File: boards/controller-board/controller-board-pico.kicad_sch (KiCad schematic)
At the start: 62 parts, among them J1 Phoenix 1935161, J2 Conn_01x02, J3 Conn_01x02, J4 Conn_01x02, J5 Conn_01x03, J6 Phoenix 1935161, J7 Conn_01x03, J8 Conn_01x03, Q1 PMV45EN, Q2 Goford_G11S_20V_11A, U2 ADS1015IRUGR, U4 RPi_Pico, U5 MCP4728

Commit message: rm photodiode, switch power terminals, 2->1 fans
* No longer using the sensor boards will just move direct connections with
thermisters taped down on bottom stand.

* Switch screw terminals to banana jacks and added jank symbol, stil WIP
  on the footprint

* Change from two smaller fans to one larger overhead fan, removing the
  drawings of the outer wings
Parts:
- removed J1: Phoenix 1935161, TerminalBlock_Phoenix:TerminalBlock_Phoenix_PT-1,5-2-5.0-H_1x02_P5.00mm_Horizontal, symbol Connector_Generic:Conn_01x02
- removed J5, J8: Conn_01x03, Connector_PinHeader_2.54mm:PinHeader_1x03_P2.54mm_Vertical, symbol Connector_Generic:Conn_01x03
- removed TP5: TestPoint-MinTH, oresat-misc:TestPoint-MinTH, symbol oresat-misc:TestPoint-MinTH
- added P1: Banana Jack V_IN, symbol controller-brd:Conn_Plug_1P
- added P2: Banana Jack GND, symbol controller-brd:Conn_Plug_1P
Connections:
- net GND: now also P2.1 (P)
- net at F1.2, F2.2, TP1.1: now also P1.1 (P)
- net PHOTODIODE: no longer names the net of U2.7 (AIN3)
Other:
- note added: "10k THT Thermistor"
- note added: "12 V Fan"
- note added: "FAN"
- note added: "Measured 12V @ 17A Rated 24A"
- note removed: "12 V Fans"
- note removed: "12V @ 11A"
- note removed: "L FAN"
- note removed: "Photodiode"
- note removed: "R FAN"
- moved on the sheet: C15, C17, C18, C19, C4, D19, F1, F2, F3, F4, HW1, HW2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

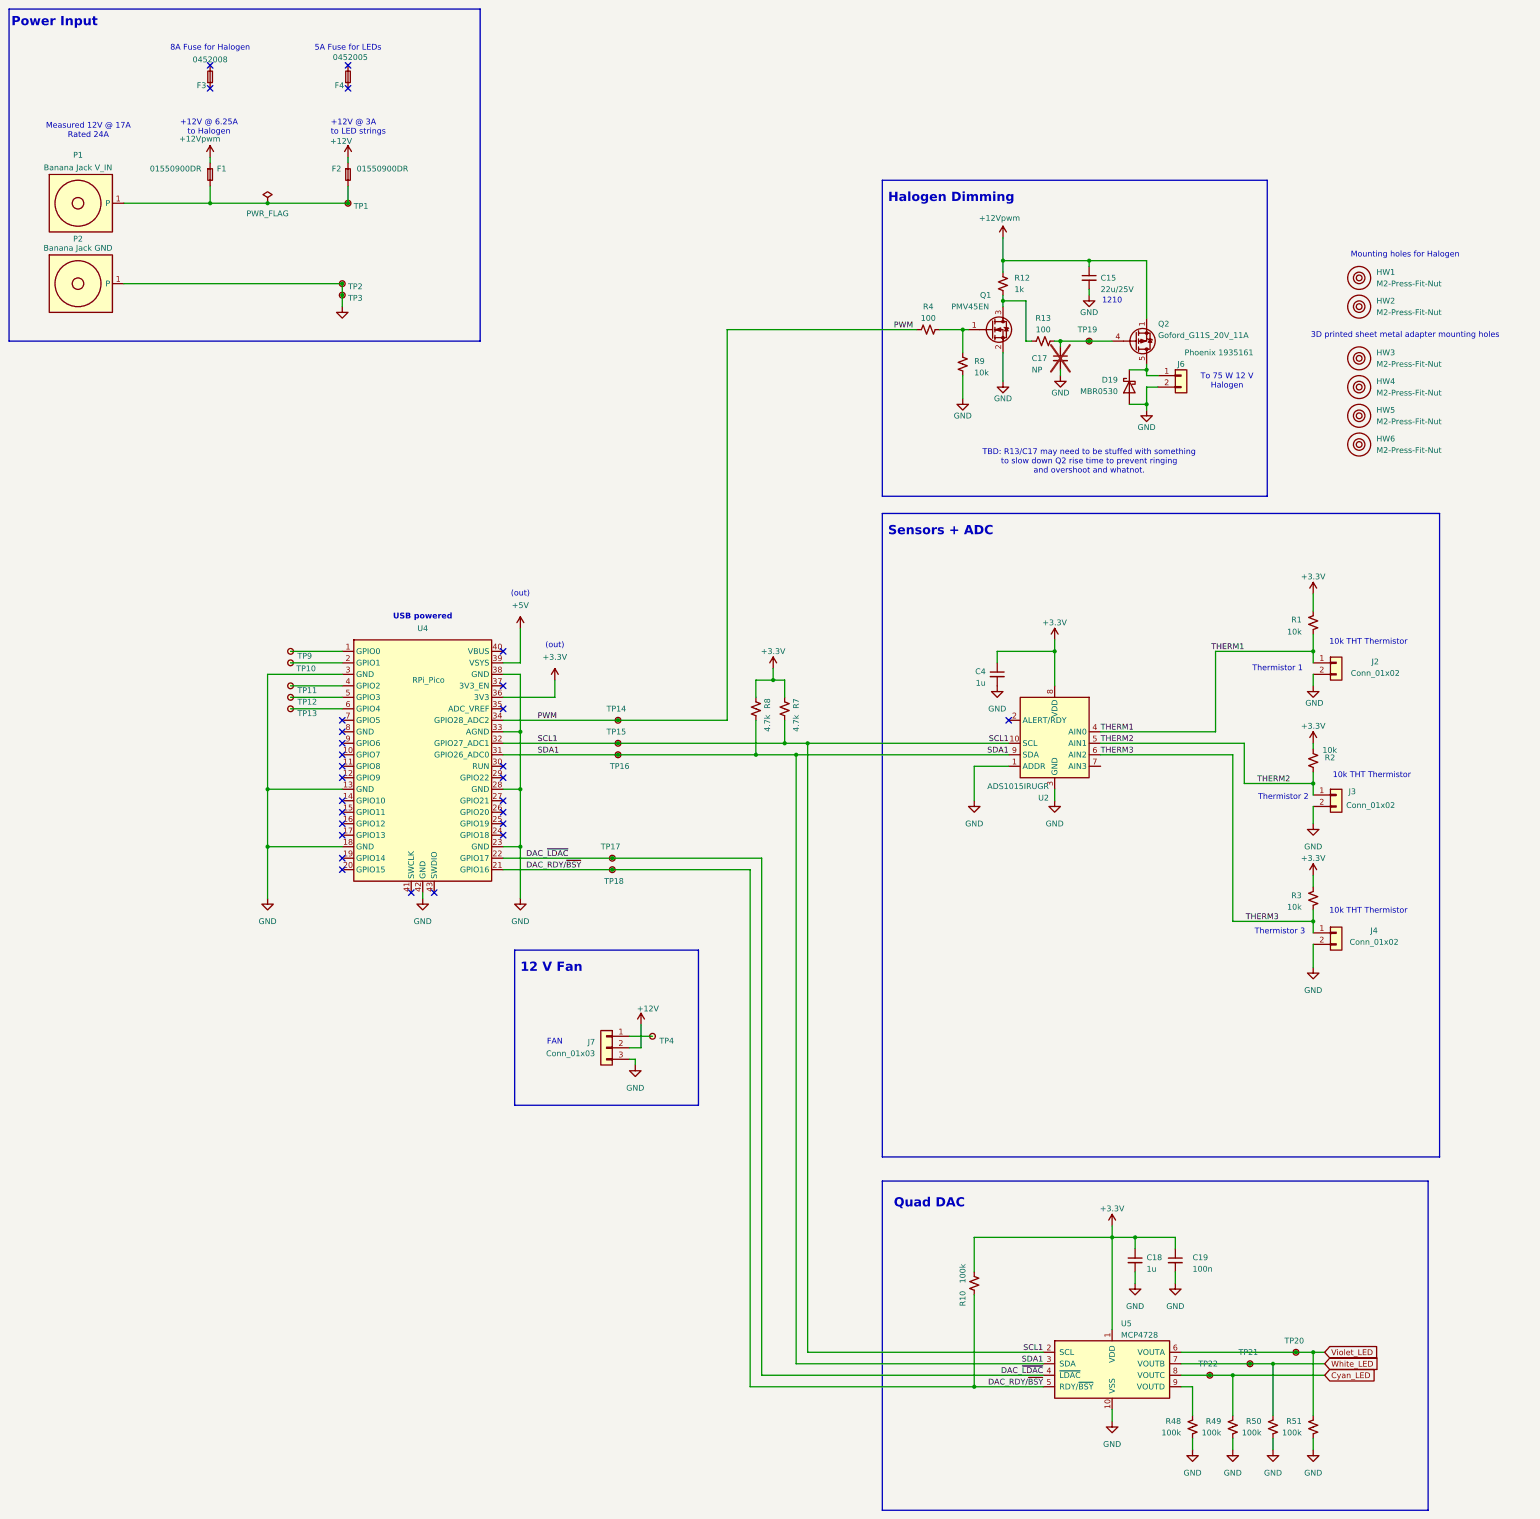
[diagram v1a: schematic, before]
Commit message: Change MCU, Power terminal, and relayout PCB
* From a pi pico we change to a RP-2040 xiao MCU which has smaller
footprint and USB-C
* Remove the previously added banana cables and go with 6PIN molex
receptacle to match the needed 12V DC powersupply we intend to use.
* With the above changes relaid out the PCB
  - No current ERC nor DRC errors of note
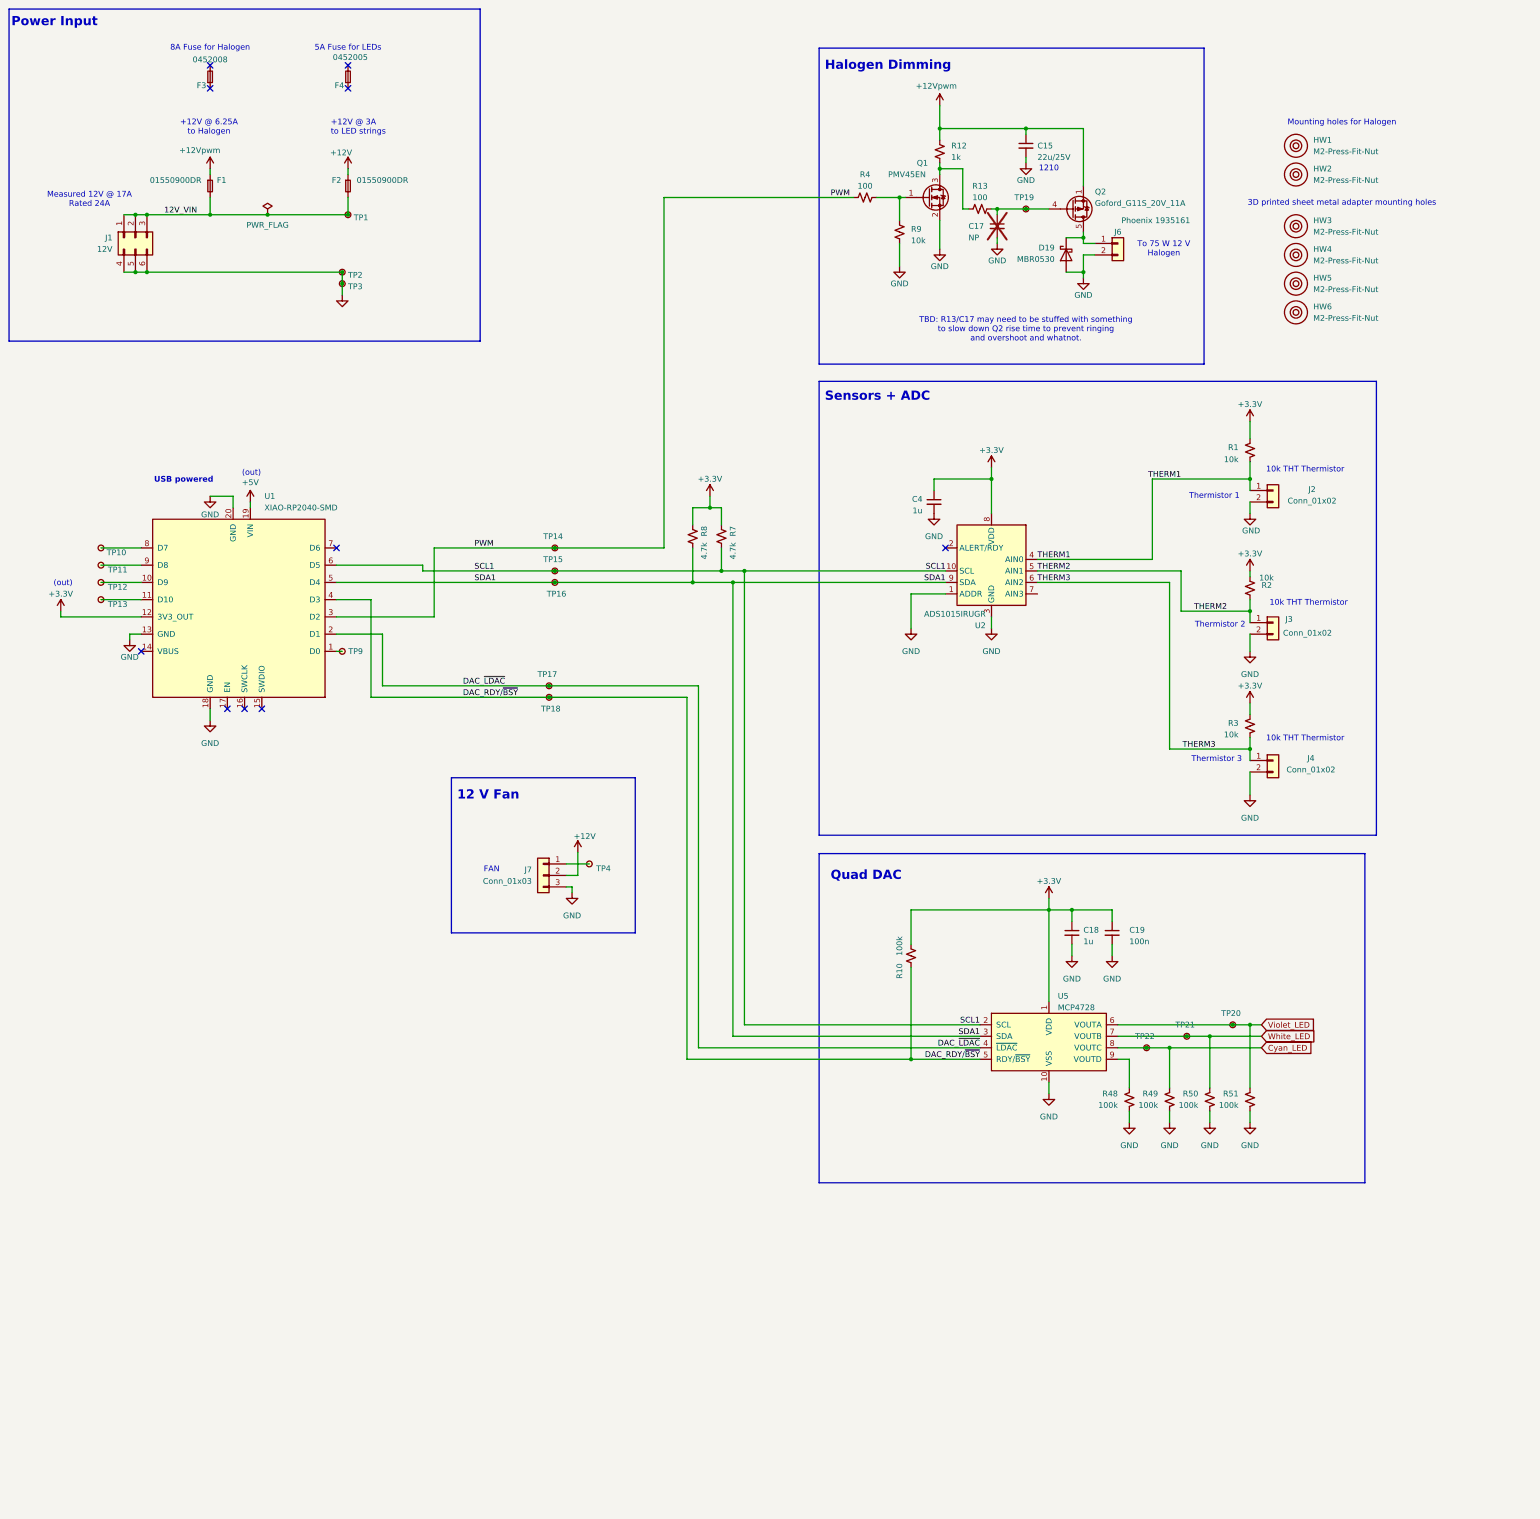
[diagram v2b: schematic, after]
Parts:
- removed P1: Banana Jack V_IN, symbol controller-brd:Conn_Plug_1P
- removed P2: Banana Jack GND, symbol controller-brd:Conn_Plug_1P
- removed U4: RPi_Pico, oresat-misc:Raspberry Pi Pico Castellated, symbol oresat-misc:RPi_Pico
- added J1: 12V, controller_brd_footprints:CONN_6P_RECPT, symbol Connector_Generic:Conn_02x03_Top_Bottom
- added U1: XIAO-RP2040-SMD, controller_brd_footprints:XIAO-RP2040-SMD, symbol controller-brd:XIAO-RP2040-SMD
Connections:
- net +3.3V: now also U1.12 (3V3_OUT)
- net +5V: now also U1.19 (VIN)
- net DAC_RDY/~{BSY}: now also U1.4 (D3)
- net DAC_~{LDAC}: now also U1.2 (D1)
- net GND: now also J1.4 (Pin_4), J1.5 (Pin_5), J1.6 (Pin_6), U1.13 (GND), U1.18 (GND), U1.20 (GND)
- net PWM: now also U1.3 (D2)
- net SCL1: now also U1.6 (D5)
- net SDA1: now also U1.5 (D4)
- net 12V_VIN: now reaches F1.2, F2.2, TP1.1
- net 12V_VIN: now also J1.1 (Pin_1), J1.2 (Pin_2), J1.3 (Pin_3)
- net at TP11.1: now also U1.9 (D8)
- net at TP12.1: now also U1.10 (D9)
- net at TP9.1: now also U1.1 (D0)
- net at TP10.1: now also U1.8 (D7)
- net at TP13.1: now also U1.11 (D10)
- no-connect marks 28 -> 10
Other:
- moved on the sheet: C15, C17, C18, C19, C4, D19, F1, F2, HW1, HW2, HW3, HW4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

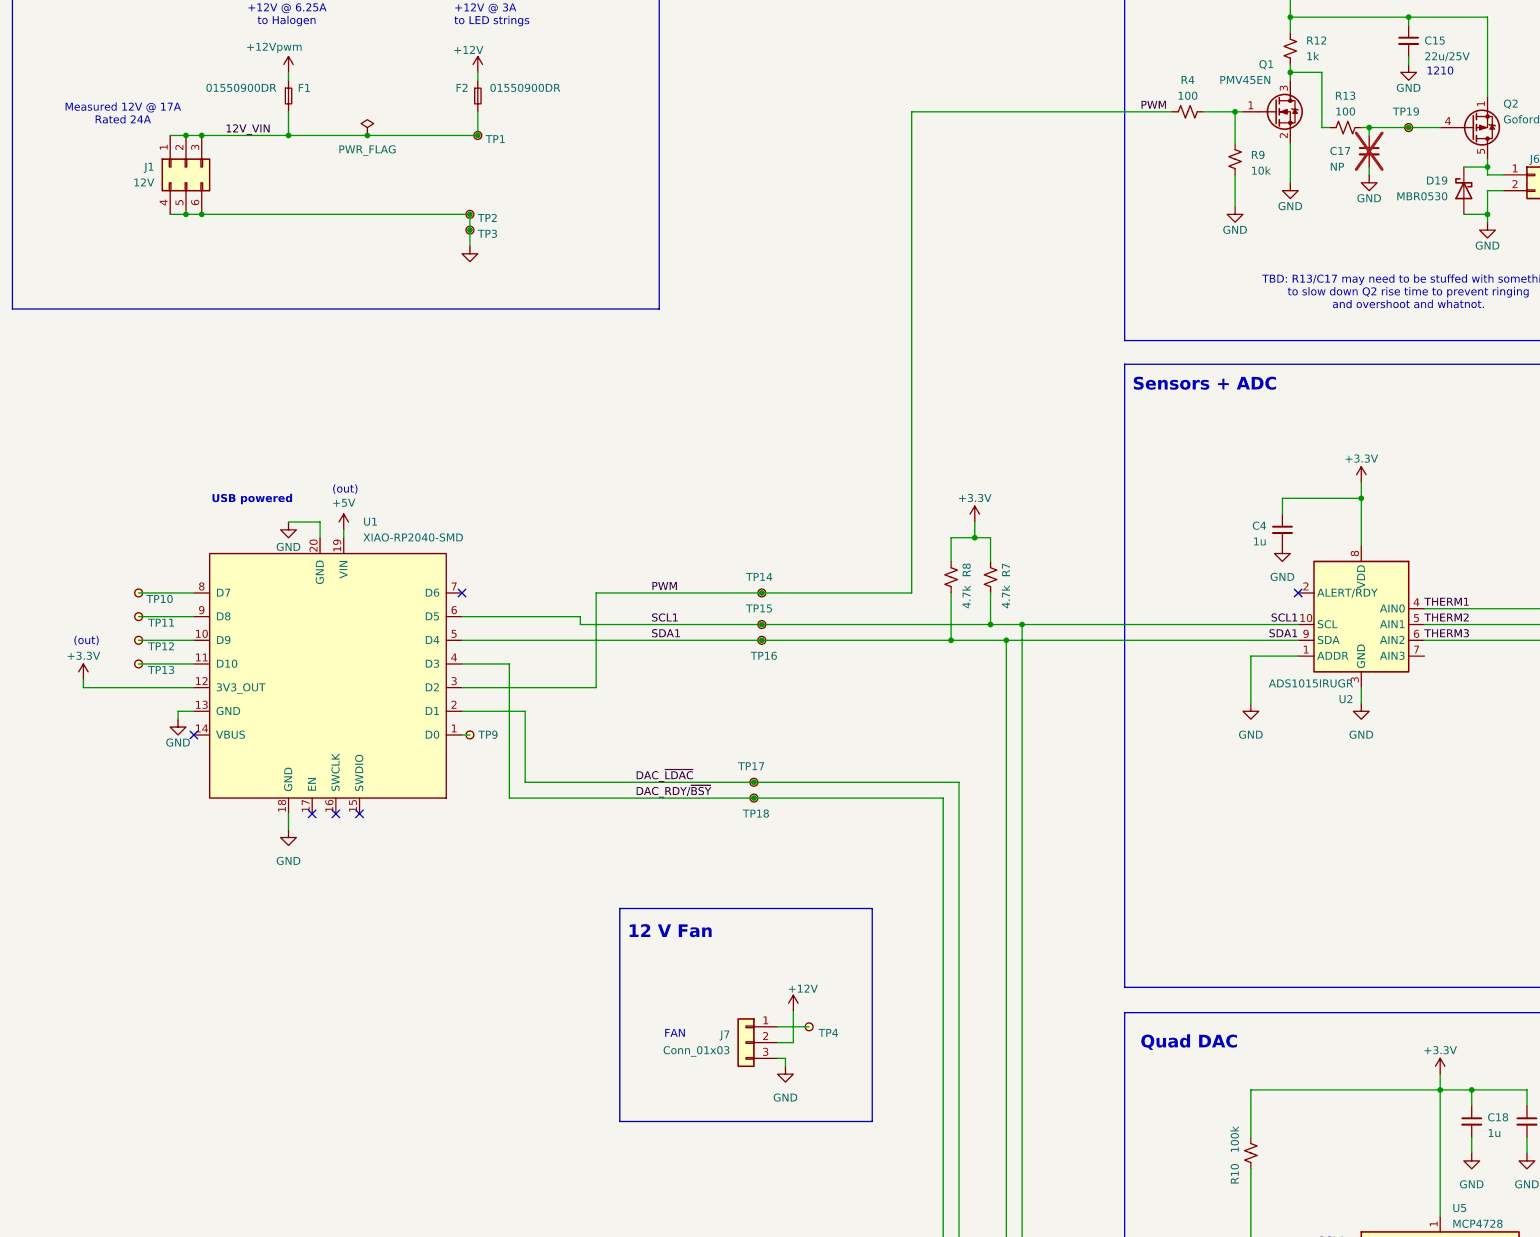
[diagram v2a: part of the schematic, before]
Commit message: Change fan connector to 4-pin PWM variant
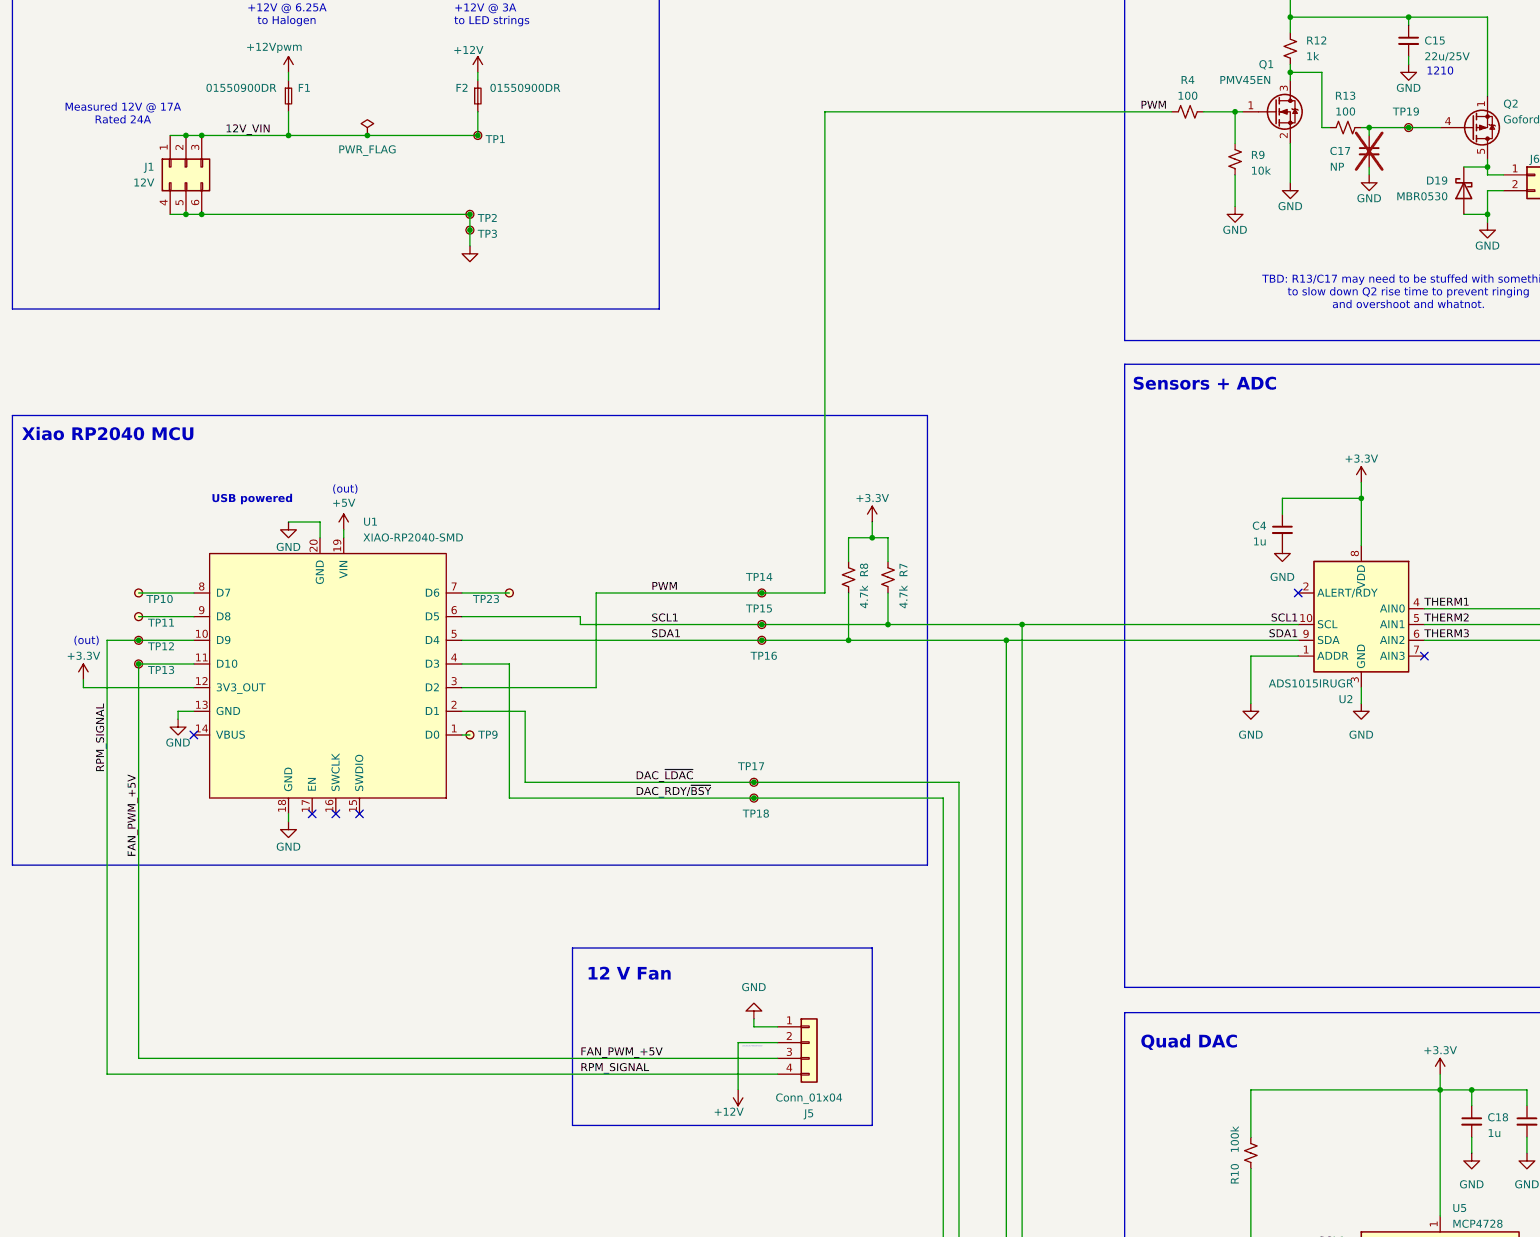
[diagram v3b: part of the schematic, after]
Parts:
- removed J7: Conn_01x03, Connector_PinHeader_2.54mm:PinHeader_1x03_P2.54mm_Vertical, symbol Connector_Generic:Conn_01x03
- removed TP4: TestPoint-MinTH, oresat-misc:TestPoint-MinTH, symbol oresat-misc:TestPoint-MinTH
- added J5: Conn_01x04, Connector_PinHeader_2.54mm:PinHeader_1x04_P2.54mm_Vertical, symbol Connector_Generic:Conn_01x04
- added TP23: TestPoint-MinTH, oresat-misc:TestPoint-MinTH, symbol oresat-misc:TestPoint-MinTH
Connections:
- net +12V: now also J5.2 (Pin_2)
- net GND: now also J5.1 (Pin_1)
- net RPM_SIGNAL: now reaches TP12.1, U1.10 (D9)
- net RPM_SIGNAL: now also J5.4 (Pin_4)
- net FAN_PWM_+5V: now reaches TP13.1, U1.11 (D10)
- net FAN_PWM_+5V: now also J5.3 (Pin_3)
- net at U1.7 (D6): now also TP23.1
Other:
- note added: "Xiao RP2040 MCU"
- note added: "just a weee bit of electrical terrorism"
- note removed: "FAN"
- moved on the sheet: R7, R8

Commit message: Cleanup, chg pin header footprint and xiao seed symbol
* Cleanup:
  - Silkscreen changed to variable values
  - added power supply digikey link in schematic
* Fan Pin header
  - added values in properties
  - caught mistake in footprint original footprint mismatching pin
    values
  - changed footprint to kicad generic 4-pin fan pin header
* Edited xiao seed manufacturer symbol to be less ugly
  - Pin spacing is closer
  - Overall symbol is now smaller
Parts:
- J5: value Conn_01x04 -> 0470531000; DPN (none) -> WM4330-ND; Distrubuter Link (none) -> https://www.digikey.com/en/products/detail/molex/0470531000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; MPN (none) -> 0470531000; Manufacturer (none) -> Molex
- U1: footprint controller_brd_footprints:XIAO-RP2040-SMD -> Seeed_Studio_XIAO_Series:XIAO-RP2040-SMD
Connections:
- net FAN_PWM_+5V: now also J5.4 (Pin_4), TP12.1, U1.10 (D9); no longer J5.3 (Pin_3), TP13.1, U1.11 (D10)
- net RPM_SIGNAL: now also J5.3 (Pin_3), TP13.1, U1.11 (D10); no longer J5.4 (Pin_4), TP12.1, U1.10 (D9)
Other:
- note added: "Measured 12V @ 17A Power supply Rated 24A Click for link"
- note added: "Xiao Seed RP2040 MCU"
- note removed: "Measured 12V @ 17A Rated 24A"
- note removed: "Xiao RP2040 MCU"
- moved on the sheet: TP10, TP11, TP12, TP13, TP23, TP9, U1
